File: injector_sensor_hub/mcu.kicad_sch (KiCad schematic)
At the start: 15 parts, among them J2 Programming Header, U1 MC2562, U2 PIC18F26K83, Y1 Crystal

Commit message: symbol fix
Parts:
- removed R5: 100R, Resistor_SMD:R_0805_2012Metric_Pad1.20x1.40mm_HandSolder, symbol Device:R_US
- added C2: 0.1uF, Capacitor_SMD:C_0805_2012Metric_Pad1.18x1.45mm_HandSolder, symbol Device:C
- added C6: 27pF, Capacitor_SMD:C_0805_2012Metric_Pad1.18x1.45mm_HandSolder, symbol Device:C
- added D?: YELLOW, LED_SMD:LED_1206_3216Metric_Pad1.42x1.75mm_HandSolder, symbol Device:LED
- added R?: 100R, Resistor_SMD:R_0805_2012Metric_Pad1.20x1.40mm_HandSolder, symbol Device:R_US
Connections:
- net +3V3: now also C2.2, R?.2
- net GND: now also C2.1, C6.2
- net LED_YELLOW: now also D?.1 (K)
- net OSC2: now also C6.1
- new net: D?.2 (A), R?.1
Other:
- note added: "12MHz"

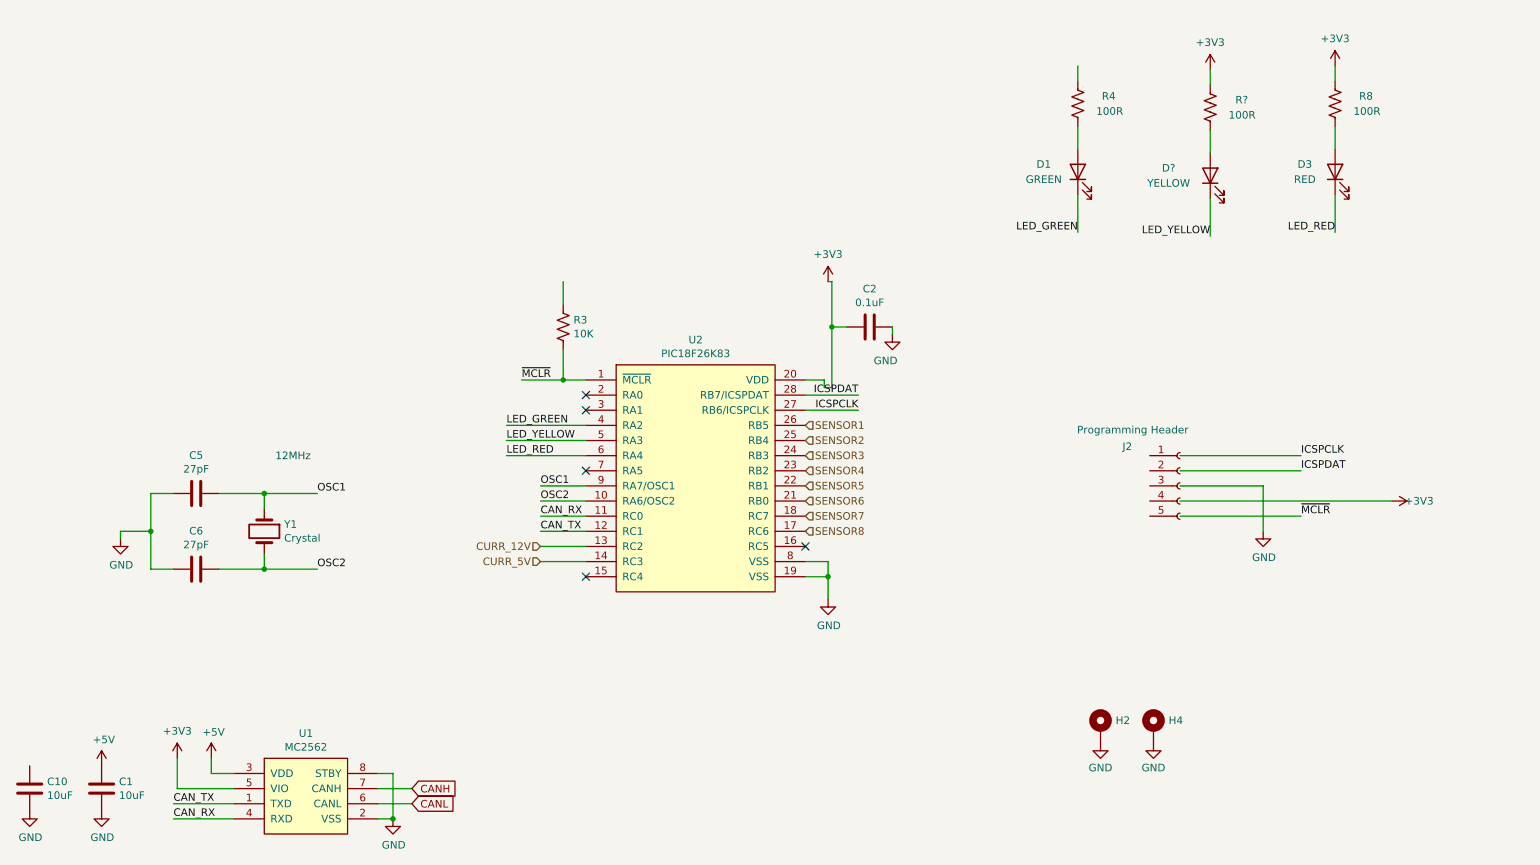
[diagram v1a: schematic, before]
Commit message: reannotate D2 LED in MCU page
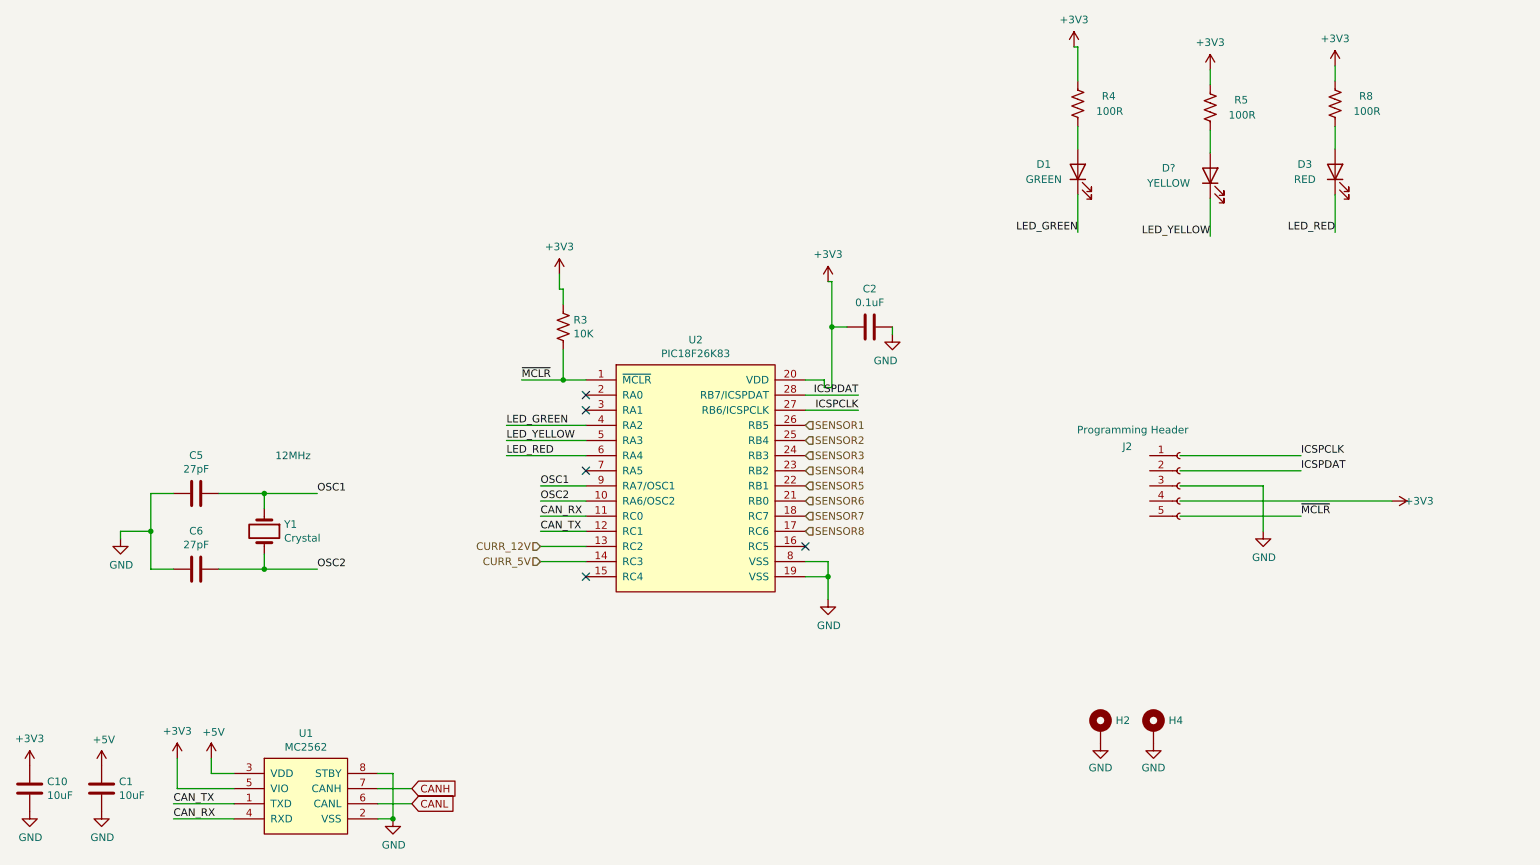
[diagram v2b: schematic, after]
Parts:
- gave numbers to parts that had none: 1
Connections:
- net +3V3: now also C10.1, R3.1, R4.2
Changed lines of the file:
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@@
 	(wire
 		(pts
+			(xy 205.105 33.02) (xy 205.105 38.735)
+		)
+		(stroke
+			(width 0)
+			(type default)
+		)
+	)
+	(wire
+		(pts
 			(xy 114.935 119.38) (xy 122.555 119.38)
 		)
@@
 	(wire
 		(pts
+			(xy 118.11 73.66) (xy 118.745 73.66)
+		)
+		(stroke
+			(width 0)
+			(type default)
+		)
+	)
+	(wire
+		(pts
 			(xy 59.69 154.94) (xy 63.5 154.94)
 		)
@@
 	(wire
 		(pts
-			(xy 118.745 72.39) (xy 118.745 76.2)
+			(xy 118.11 71.12) (xy 118.11 73.66)
 		)
 		(stroke
@@
 	(wire
 		(pts
-			(xy 248.285 38.735) (xy 248.285 36.195)
+			(xy 118.745 73.66) (xy 118.745 76.2)
 		)
 		(stroke
@@
 	(wire
 		(pts
-			(xy 205.105 38.735) (xy 205.105 36.195)
+			(xy 248.285 38.735) (xy 248.285 36.195)
 		)
 		(stroke
@@
 	(wire
 		(pts
+			(xy 204.47 33.02) (xy 205.105 33.02)
+		)
+		(stroke
+			(width 0)
+			(type default)
+		)
+	)
+	(wire
+		(pts
 			(xy 222.25 101.6) (xy 242.57 101.6)
 		)
@@
 	)
 	(symbol
+		(lib_name "+3V3_1")
+		(lib_id "power:+3V3")
+		(at 29.21 153.67 0)
+		(unit 1)
+		(exclude_from_sim no)
+		(in_bom yes)
+		(on_board yes)
+		(dnp no)
+		(property "Reference" "#PWR025"
+			(at 29.21 157.48 0)
+			(effects
+				(font
+					(size 1.27 1.27)
+				)
+				(hide yes)
+			)
+		)
+		(property "Value" "+3V3"
+			(at 29.21 149.098 0)
+			(effects
+				(font
+					(size 1.27 1.27)
+				)
+			)
+		)
+		(property "Footprint" ""
+			(at 29.21 153.67 0)
+			(effects
+				(font
+					(size 1.27 1.27)
+				)
+				(hide yes)
+			)
+		)
+		(property "Datasheet" ""
+			(at 29.21 153.67 0)
+			(effects
+				(font
+					(size 1.27 1.27)
+				)
+				(hide yes)
+			)
+		)
+		(property "Description" ""
+			(at 29.21 153.67 0)
+			(effects
+				(font
+					(size 1.27 1.27)
+				)
+				(hide yes)
+			)
+		)
+		(pin "1"
+		)
+		(instances
+			(project "injector_sensor_hub"
+				(path "/65b6af08-52d0-4269-bf55-02b67cf42271/39ac2d46-be06-492f-bec7-ce85b54c0a9a"
+					(reference "#PWR025")
+					(unit 1)
+				)
+			)
+		)
+	)
+	(symbol
 		(lib_id "power:GND")
 		(at 44.45 115.57 0)
@@
 		(on_board yes)
 		(dnp no)
-		(property "Reference" "R?"
+		(property "Reference" "R5"
 			(at 233.68 41.91 0)
 			(effects
@@
 			(project "injector_sensor_hub"
 				(path "/65b6af08-52d0-4269-bf55-02b67cf42271/39ac2d46-be06-492f-bec7-ce85b54c0a9a"
-					(reference "R?")
+					(reference "R5")
 					(unit 1)
 				)
@@
 	)
 	(symbol
+		(lib_name "+3V3_1")
+		(lib_id "power:+3V3")
+		(at 204.47 33.02 0)
+		(unit 1)
+		(exclude_from_sim no)
+		(in_bom yes)
+		(on_board yes)
+		(dnp no)
+		(property "Reference" "#PWR064"
+			(at 204.47 36.83 0)
+			(effects
+				(font
+					(size 1.27 1.27)
+				)
+				(hide yes)
+			)
+		)
+		(property "Value" "+3V3"
+			(at 204.47 28.448 0)
+			(effects
+				(font
+					(size 1.27 1.27)
+				)
+			)
+		)
+		(property "Footprint" ""
+			(at 204.47 33.02 0)
+			(effects
+				(font
+					(size 1.27 1.27)
+				)
+				(hide yes)
+			)
+		)
+		(property "Datasheet" ""
+			(at 204.47 33.02 0)
+			(effects
+				(font
+					(size 1.27 1.27)
+				)
+				(hide yes)
+			)
+		)
+		(property "Description" ""
+			(at 204.47 33.02 0)
+			(effects
+				(font
+					(size 1.27 1.27)
+				)
+				(hide yes)
+			)
+		)
+		(pin "1"
+		)
+		(instances
+			(project "injector_sensor_hub"
+				(path "/65b6af08-52d0-4269-bf55-02b67cf42271/39ac2d46-be06-492f-bec7-ce85b54c0a9a"
+					(reference "#PWR064")
+					(unit 1)
+				)
+			)
+		)
+	)
+	(symbol
 		(lib_id "Device:C")
 		(at 57.15 107.95 270)
@@
 					(unit 1)
 				)
+			)
+		)
+	)
+	(symbol
+		(lib_name "+3V3_1")
+		(lib_id "power:+3V3")
+		(at 118.11 71.12 0)
+		(unit 1)
+		(exclude_from_sim no)
+		(in_bom yes)
+		(on_board yes)
+		(dnp no)
+		(property "Reference" "#PWR013"
+			(at 118.11 74.93 0)
+			(effects
+				(font
+					(size 1.27 1.27)
+				)
+				(hide yes)
+			)
+		)
+		(property "Value" "+3V3"
+			(at 118.11 66.548 0)
+			(effects
+				(font
+					(size 1.27 1.27)
+				)
+			)
+		)
+		(property "Footprint" ""
+			(at 118.11 71.12 0)
+			(effects
+				(font
+					(size 1.27 1.27)
+				)
+				(hide yes)
+			)
+		)
+		(property "Datasheet" ""
+			(at 118.11 71.12 0)
+			(effects
+				(font
+					(size 1.27 1.27)
+				)
+				(hide yes)
+			)
+		)
+		(property "Description" ""
+			(at 118.11 71.12 0)
+			(effects
+				(font
+					(size 1.27 1.27)
+				)
+				(hide yes)
+			)
+		)
+		(pin "1"
+		)
+		(instances
+			(project "injector_sensor_hub"
+				(path "/65b6af08-52d0-4269-bf55-02b67cf42271/39ac2d46-be06-492f-bec7-ce85b54c0a9a"
+					(reference "#PWR013")
+					(unit 1)
+				)

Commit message: fixed programming header lol
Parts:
- gave numbers to parts that had none: 1
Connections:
- net +3V3: now also J2.4 (Pin_4)
- net GND: now also J2.3 (Pin_3)
- net ICSPCLK: now also J2.1 (Pin_1)
- net ICSPDAT: now also J2.2 (Pin_2)
- net ~{MCLR}: now also J2.5 (Pin_5)
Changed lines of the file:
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@@
 	(wire
 		(pts
-			(xy 60.96 120.65) (xy 68.58 120.65)
+			(xy 196.85 106.68) (xy 217.17 106.68)
 		)
 		(stroke
@@
 	(wire
 		(pts
-			(xy 236.22 106.68) (xy 236.22 114.3)
+			(xy 60.96 120.65) (xy 68.58 120.65)
 		)
 		(stroke
@@
 	(wire
 		(pts
-			(xy 87.63 160.02) (xy 93.345 160.02)
+			(xy 190.5 111.76) (xy 217.17 111.76)
 		)
 		(stroke
@@
 	(wire
 		(pts
-			(xy 242.57 104.14) (xy 222.25 104.14)
+			(xy 87.63 160.02) (xy 93.345 160.02)
 		)
 		(stroke
@@
 	(wire
 		(pts
+			(xy 199.39 104.14) (xy 217.17 104.14)
+		)
+		(stroke
+			(width 0)
+			(type default)
+		)
+	)
+	(wire
+		(pts
 			(xy 109.22 101.6) (xy 122.555 101.6)
 		)
@@
 	(wire
 		(pts
-			(xy 222.25 109.22) (xy 257.81 109.22)
+			(xy 199.39 101.6) (xy 217.17 101.6)
 		)
 		(stroke
@@
 	(wire
 		(pts
-			(xy 222.25 106.68) (xy 236.22 106.68)
+			(xy 109.22 96.52) (xy 122.555 96.52)
 		)
 		(stroke
@@
 	(wire
 		(pts
-			(xy 109.22 96.52) (xy 122.555 96.52)
+			(xy 114.935 116.84) (xy 122.555 116.84)
 		)
 		(stroke
@@
 	(wire
 		(pts
-			(xy 114.935 116.84) (xy 122.555 116.84)
+			(xy 53.34 107.95) (xy 49.53 107.95)
 		)
 		(stroke
@@
 	(wire
 		(pts
-			(xy 53.34 107.95) (xy 49.53 107.95)
+			(xy 162.56 90.17) (xy 162.56 88.9)
 		)
 		(stroke
@@
 	(wire
 		(pts
-			(xy 162.56 90.17) (xy 162.56 88.9)
+			(xy 114.935 111.76) (xy 122.555 111.76)
 		)
 		(stroke
@@
 	(wire
 		(pts
-			(xy 114.935 111.76) (xy 122.555 111.76)
+			(xy 59.69 152.4) (xy 59.69 154.94)
 		)
 		(stroke
@@
 	(wire
 		(pts
-			(xy 59.69 152.4) (xy 59.69 154.94)
+			(xy 196.85 115.57) (xy 196.85 106.68)
 		)
 		(stroke
@@
 	(wire
 		(pts
-			(xy 222.25 111.76) (xy 242.57 111.76)
+			(xy 201.93 109.22) (xy 217.17 109.22)
 		)
 		(stroke
@@
 	(wire
 		(pts
-			(xy 222.25 101.6) (xy 242.57 101.6)
-		)
-		(stroke
-			(width 0)
-			(type default)
-		)
-	)
-	(wire
-		(pts
 			(xy 77.47 120.65) (xy 68.58 120.65)
 		)
@@
 	)
 	(label "ICSPDAT"
-		(at 242.57 104.14 0)
+		(at 199.39 104.14 0)
 		(fields_autoplaced yes)
 		(effects
@@
 	)
 	(label "ICSPCLK"
-		(at 242.57 101.6 0)
+		(at 199.39 101.6 0)
 		(fields_autoplaced yes)
 		(effects
@@
 	)
 	(label "~{MCLR}"
-		(at 242.57 111.76 0)
+		(at 190.5 111.76 0)
 		(fields_autoplaced yes)
 		(effects
@@
 		(dnp no)
 		(property "Reference" "J2"
-			(at 212.598 100.076 0)
+			(at 217.17 96.012 0)
 			(effects
 				(font
@@
 		)
 		(property "Value" "Programming Header"
-			(at 204.978 97.282 0)
+			(at 206.248 92.71 0)
 			(effects
 				(font
@@
 	(symbol
 		(lib_id "power:GND")
-		(at 236.22 114.3 0)
+		(at 196.85 115.57 0)
 		(unit 1)
 		(exclude_from_sim no)
@@
 		(dnp no)
 		(property "Reference" "#PWR06"
-			(at 236.22 120.65 0)
+			(at 196.85 121.92 0)
 			(effects
 				(font
@@
 		)
 		(property "Value" "GND"
-			(at 236.347 118.6942 0)
+			(at 196.85 119.634 0)
 			(effects
 				(font
@@
 		)
 		(property "Footprint" ""
-			(at 236.22 114.3 0)
+			(at 196.85 115.57 0)
 			(effects
 				(font
@@
 		)
 		(property "Datasheet" ""
-			(at 236.22 114.3 0)
+			(at 196.85 115.57 0)
 			(effects
 				(font
@@
 		)
 		(property "Description" ""
-			(at 236.22 114.3 0)
+			(at 196.85 115.57 0)
 			(effects
 				(font
@@
 		(lib_name "+3V3_1")
 		(lib_id "power:+3V3")
-		(at 257.81 109.22 270)
+		(at 201.93 109.22 90)
 		(unit 1)
 		(exclude_from_sim no)
@@
 		(dnp no)
 		(property "Reference" "#PWR011"
-			(at 254 109.22 0)
+			(at 205.74 109.22 0)
 			(effects
 				(font
@@
 		)
 		(property "Value" "+3V3"
-			(at 262.382 109.22 90)
+			(at 203.2 108.204 90)
 			(effects
 				(font
@@
 		)
 		(property "Footprint" ""
-			(at 257.81 109.22 0)
+			(at 201.93 109.22 0)
 			(effects
 				(font
@@
 		)
 		(property "Datasheet" ""
-			(at 257.81 109.22 0)
+			(at 201.93 109.22 0)
 			(effects
 				(font
@@
 		)
 		(property "Description" ""
-			(at 257.81 109.22 0)
+			(at 201.93 109.22 0)
 			(effects
 				(font
@@
 		(on_board yes)
 		(dnp no)
-		(property "Reference" "D?"
+		(property "Reference" "D2"
 			(at 220.345 53.34 90)
 			(effects
@@
 			(project "injector_sensor_hub"
 				(path "/65b6af08-52d0-4269-bf55-02b67cf42271/39ac2d46-be06-492f-bec7-ce85b54c0a9a"
-					(reference "D?")
+					(reference "D2")
 					(unit 1)
 				)

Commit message: changed from 3v3 to 5v
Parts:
- removed C10: 10uF, Capacitor_SMD:C_0805_2012Metric_Pad1.18x1.45mm_HandSolder, symbol Device:C
- U1: value MC2562 -> MCP2562
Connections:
- net +3V3 is gone; now on net +5V: C2.2, J2.4 (Pin_4), R3.1, R4.2, R5.2, R8.2, U1.5 (VIO), U2.20 (VDD)

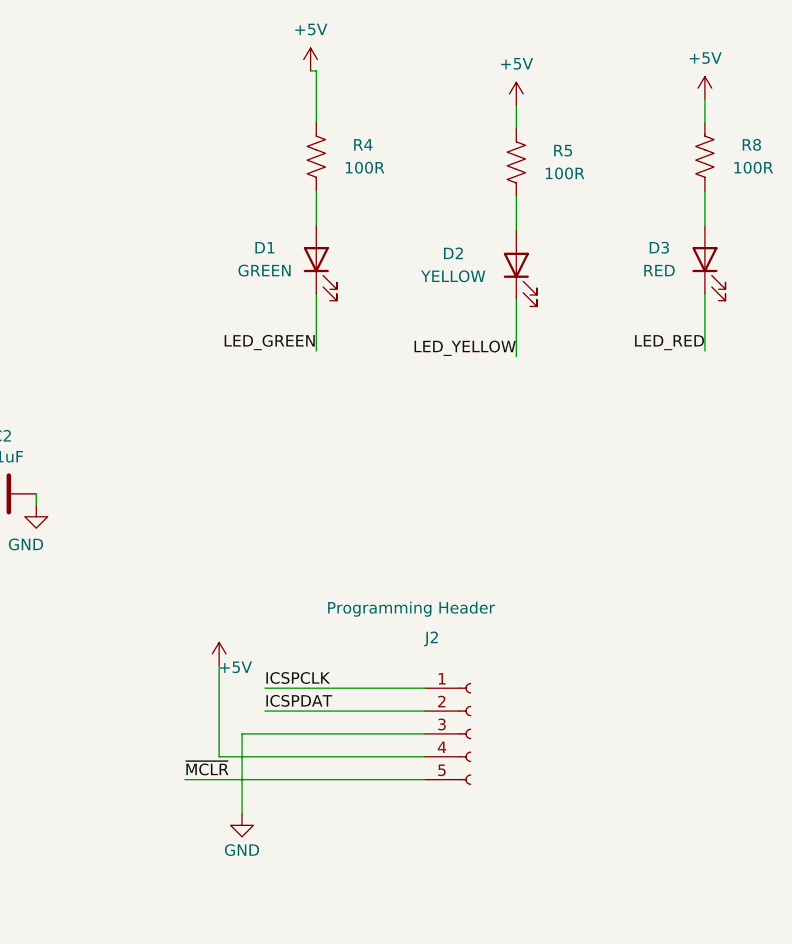
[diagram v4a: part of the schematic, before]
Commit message: upgraded resistors on LEDs
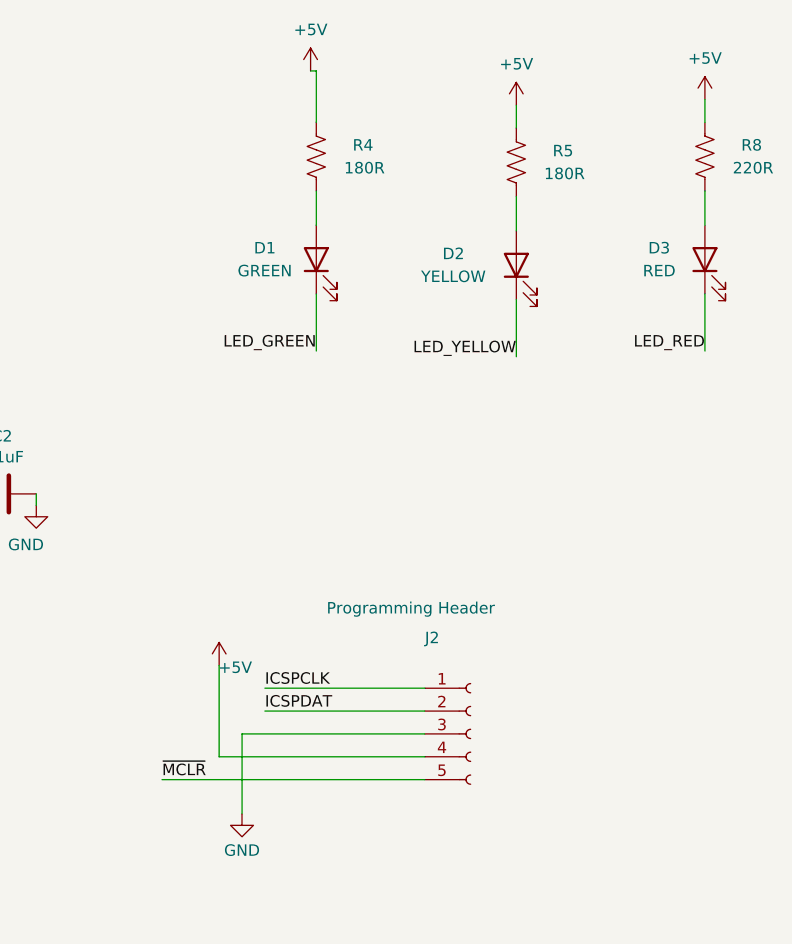
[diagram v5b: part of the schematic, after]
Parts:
- R4, R5: value 100R -> 180R
- R8: value 100R -> 220R
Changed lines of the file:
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@@
 	(wire
 		(pts
-			(xy 190.5 111.76) (xy 217.17 111.76)
+			(xy 187.96 111.76) (xy 217.17 111.76)
 		)
 		(stroke
@@
 	)
 	(label "~{MCLR}"
-		(at 190.5 111.76 0)
+		(at 187.96 111.76 0)
 		(fields_autoplaced yes)
 		(effects
@@
 			)
 		)
-		(property "Value" "100R"
+		(property "Value" "180R"
 			(at 212.725 43.815 0)
 			(effects
@@
 			)
 		)
-		(property "Value" "100R"
+		(property "Value" "220R"
 			(at 255.905 43.815 0)
 			(effects
@@
 			)
 		)
-		(property "Value" "100R"
+		(property "Value" "180R"
 			(at 234.95 44.45 0)
 			(effects

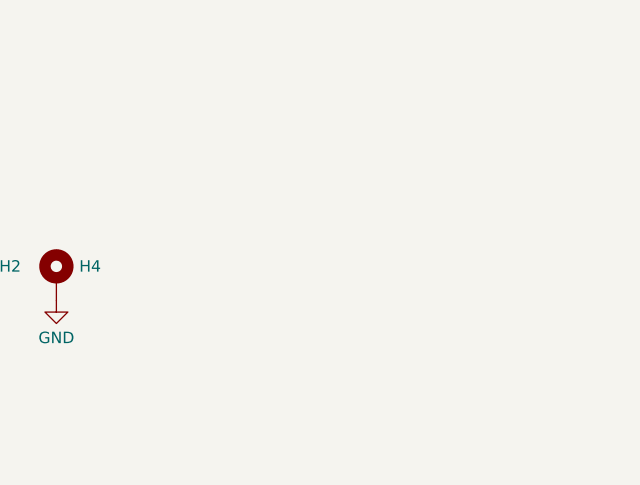
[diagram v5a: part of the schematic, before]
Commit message: added sensor designation markup
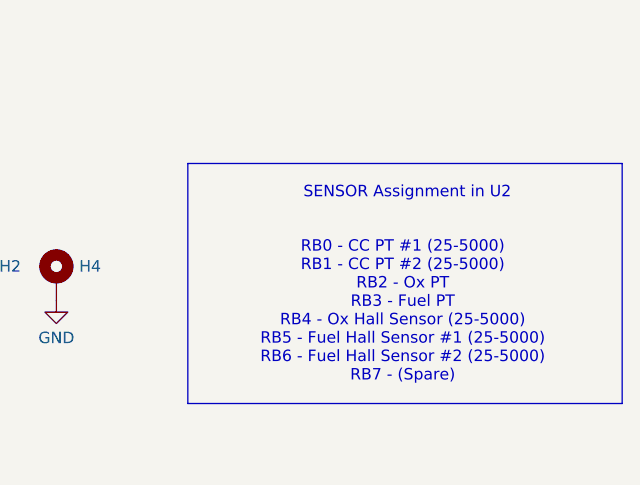
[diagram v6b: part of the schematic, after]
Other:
- note added: "RB0 - CC PT #1 (25-5000) RB1 - CC PT #2 (25-5000) RB2 - Ox PT RB3 - Fuel PT RB4 - Ox Hall Sensor (25-5000) RB5 - Fuel Hall Sensor #1 (25-5000) RB6 - Fuel Hall Sensor #2 (25-5000) RB7 - (Spare)"
- note added: "SENSOR Assignment in U2"
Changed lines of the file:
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@@
+		)
+	)
+	(rectangle
+		(start 232.41 134.62)
+		(end 280.67 161.29)
+		(stroke
+			(width 0)
+			(type default)
+		)
+		(fill
+			(type none)
+		)
+	)
+	(text "SENSOR Assignment in U2\n"
+		(exclude_from_sim no)
+		(at 256.794 137.922 0)
+		(effects
+			(font
+				(size 1.27 1.27)
+			)
+		)
+	)
+	(text "RB0 - CC PT #1 (25-5000)\nRB1 - CC PT #2 (25-5000)\nRB2 - Ox PT\nRB3 - Fuel PT\nRB4 - Ox Hall Sensor (25-5000)\nRB5 - Fuel Hall Sensor #1 (25-5000)\nRB6 - Fuel Hall Sensor #2 (25-5000)\nRB7 - (Spare)\n\n"
+		(exclude_from_sim no)
+		(at 256.286 152.146 0)
+		(effects
+			(font
+				(size 1.27 1.27)
+			)
 		)
 	)
